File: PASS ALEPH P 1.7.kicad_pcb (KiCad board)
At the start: 2 copper layers, 200 x 100 mm, 79 parts, among them Q1 BCX56-16,115, Q10 BCX56-16,115, Q2 BCX53-16,115, Q3 610, Q4 610, Q5 9610, Q6 9610, Q7 610, Q8 610, Q9 BCX53-16,115

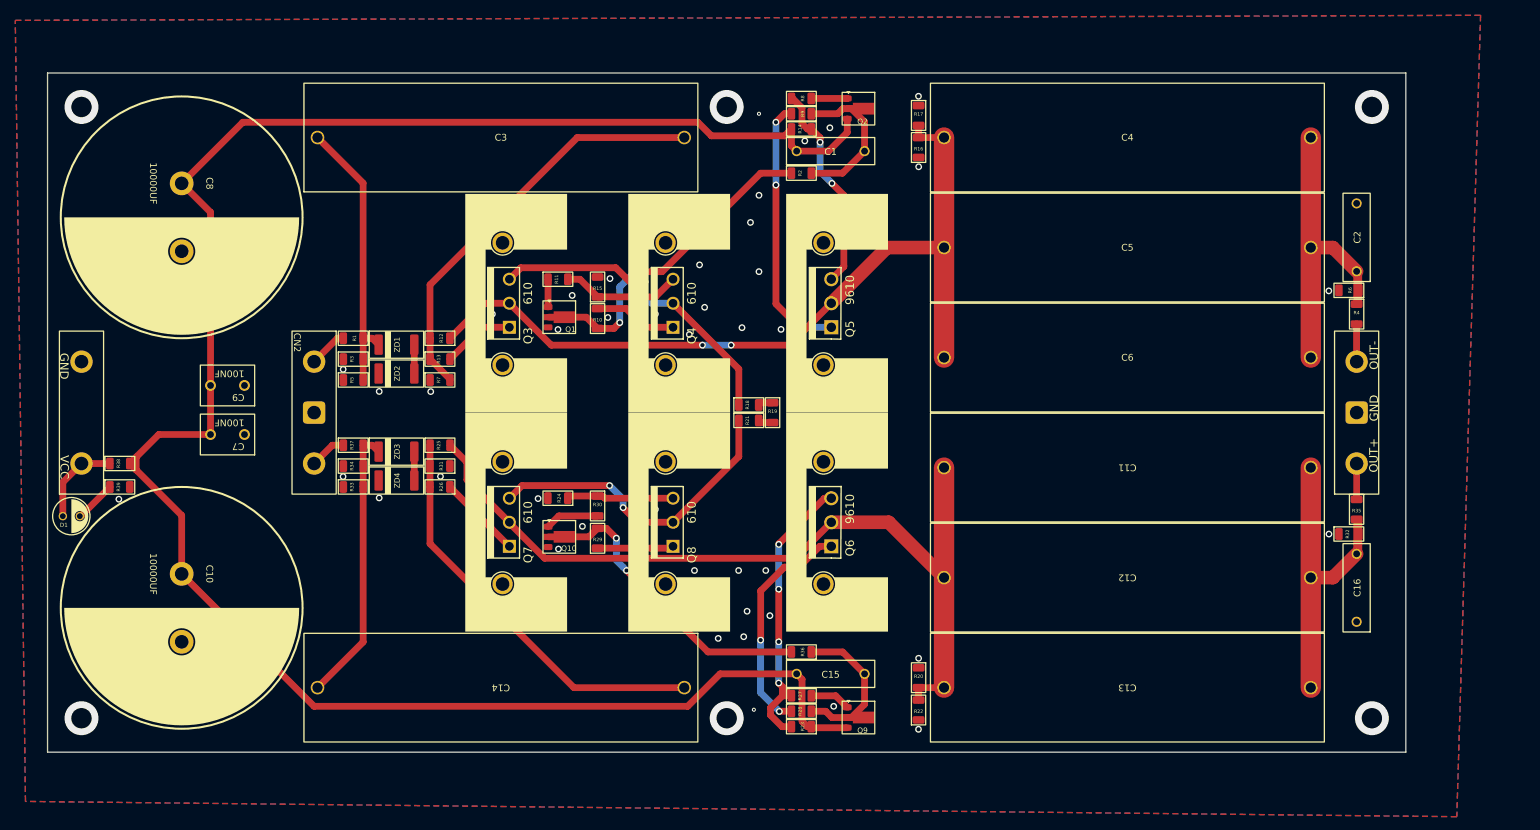
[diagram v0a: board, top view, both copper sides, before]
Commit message: 6 layer-board, layout finished
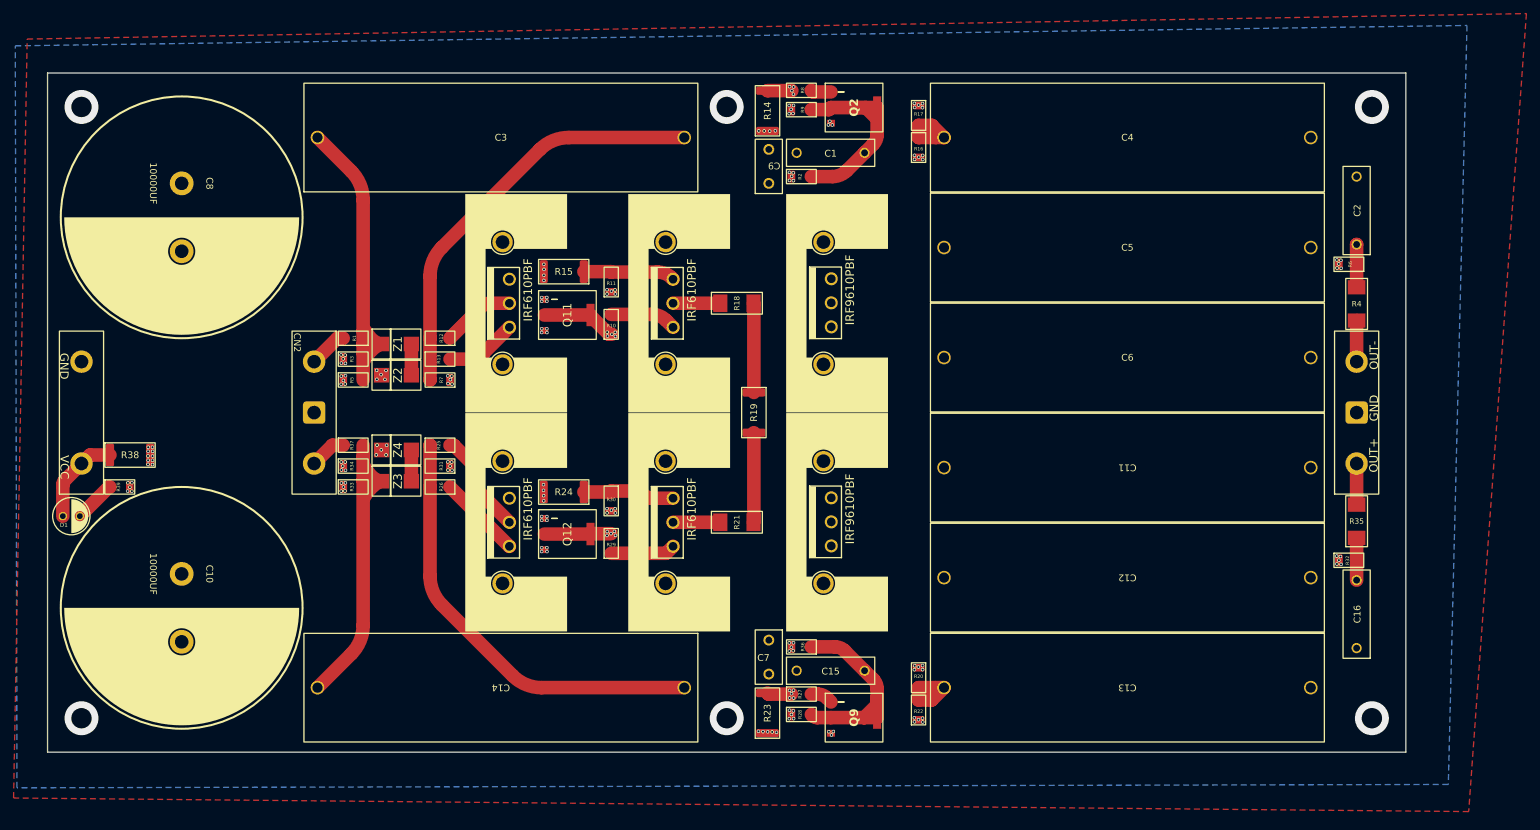
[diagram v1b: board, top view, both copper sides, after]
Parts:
- removed Q1, Q10: BCX56-16,115, 3rd package:BCX56-16,115
- added Q11: BCP56-16,115, cus_transistor:BCP56-16,115, F.Cu at (96.3, 73.4)
- added Q12: BCP56-16,115, cus_transistor:BCP56-16,115, F.Cu at (96.3, 105.6)
- C7, C9: footprint 3rd package:MES104J2A-7-50R0 -> cus_capacitor:MES104J2A-7-50R0
- Q2, Q9: footprint 3rd package:BCX53-16,115 -> cus_transistor:BCP53-16,115
- Q3, Q4, Q7, Q8: value 610 -> IRF610PBF; footprint 3rd package:IRF610PBF -> cus_mosfet:IRF610PBF
- Q5, Q6: value 9610 -> IRF9610PBF; footprint 3rd package:IRF9610PBF -> cus_mosfet:IRF9610PBF
- R1, R37: value 0 -> 10K
- R14, R23, R38: footprint generic package:R_1206 -> generic package:R 2512
- R15, R24: value 33.1 -> 33.2; footprint generic package:R_1206 -> generic package:R 2512
- R18, R21, R35, R4: footprint generic package:R_1206 -> cus_resistor:R_MELF_0207
- R19: footprint generic package:R_1206 -> cus_resistor:R_2512
- Z1: renamed from ZD1; value ZMY9V1-GS08 -> 1SMB5924BT3G; footprint 3rd package:ZMY9V1-GS08 -> cus_zener:1SMB5924BT3G
- Z2: renamed from ZD2; value ZMY9V1-GS08 -> 1SMB5924BT3G; footprint 3rd package:ZMY9V1-GS08 -> cus_zener:1SMB5924BT3G
- Z3: renamed from ZD3; value ZMY9V1-GS08 -> 1SMB5924BT3G; footprint 3rd package:ZMY9V1-GS08 -> cus_zener:1SMB5924BT3G
- Z4: renamed from ZD4; value ZMY9V1-GS08 -> 1SMB5924BT3G; footprint 3rd package:ZMY9V1-GS08 -> cus_zener:1SMB5924BT3G
- moved C7 82.9 mm to (126.0, 121.2), turned to -90 degrees
- moved C9 82.7 mm to (126.0, 54.0), turned to 90 degrees
- moved R21 15.1 mm to (121.2, 103.9)
- moved R18 15.1 mm to (121.2, 71.7)
- moved R11 7.86 mm to (102.8, 68.5), turned to 90 degrees
- moved R23 5.08 mm to (125.8, 135.0), turned to 90 degrees
- moved R14 5.00 mm to (125.8, 46.3), turned to 90 degrees
- moved Z4 4.50 mm to (71.1, 93.2)
- moved Z3 4.35 mm to (71.1, 97.8)
- moved R19 4.05 mm to (123.8, 84.8)
- moved C2 3.95 mm to (212.5, 58.0)
- moved R24 3.93 mm to (98.7, 99.4)
- moved C16 3.88 mm to (212.5, 117.4)
- moved R32 3.87 mm to (211.4, 109.5)
- moved R6 3.84 mm to (211.4, 65.9)
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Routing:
- net Net-(Q2-E): track 297.6 -> 0.00 mm, vias 0 -> 25
- net Net-(Q3-D): track 121.3 -> 20.8 mm, vias 2 -> 0
- net Net-(Q6-D): track 124.8 -> 25.2 mm
- net Net-(C11-Pad1): track 51.0 -> 6.23 mm
- net Net-(C2-Pad1): track 50.5 -> 6.31 mm
- net Net-(Q7-S): track 46.8 -> 35.2 mm, vias 2 -> 0
- net Net-(R19-Pad2): track 2.17 -> 13.2 mm
- net Net-(R18-Pad2): track 2.17 -> 13.2 mm
- net Net-(Q3-S): track 46.0 -> 36.0 mm, vias 1 -> 0
- net Net-(Q9-C): track 22.7 -> 30.3 mm
- net Net-(Q2-C): track 22.5 -> 29.9 mm
- net Net-(Q11-B): track 4.09 -> 10.6 mm, vias 0 -> 9
- net Net-(Q6-S): track 43.6 -> 37.2 mm, vias 4 -> 5
- net Net-(Q5-S): track 31.0 -> 36.8 mm, vias 2 -> 4
- net Net-(Q4-S): track 17.6 -> 13.5 mm
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- added copper zone on In1.Cu, net GND
- added copper zone on In2.Cu, net GND
- added copper zone on In3.Cu, net GND
- added copper zone on In4.Cu, net GND
- added copper zone on In4.Cu, net Net-(C11-Pad1)
- added copper zone on In4.Cu, net Net-(C2-Pad1)
- added copper zone on In4.Cu, net Net-(Q2-E)
- added copper zone on In4.Cu, net Net-(Q3-D)
- added copper zone on In4.Cu, net Net-(Q6-D)
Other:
- copper layers 2 -> 6

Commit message: replace some film resistor, fix some bug
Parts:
- R1, R16, R2, R22, R36, R37: footprint generic package:R_1206 -> cus_resistor:R_MELF_0207
- R14, R23: value 22.1 -> 22; footprint generic package:R 2512 -> cus_resistor:R_MELF_0207
- R15, R24: value 33.2 -> 33; footprint generic package:R 2512 -> cus_resistor:R_MELF_0207
- R38: footprint generic package:R 2512 -> cus_resistor:R_MELF_0207
- moved R17 7.48 mm to (147.5, 51.5), turned to 90 degrees
- moved R37 6.10 mm to (63.2, 98.5)
- moved R16 4.00 mm to (147.5, 44.8), turned to -90 degrees
- moved R33 3.70 mm to (64.8, 95.0)
- moved R34 3.38 mm to (64.8, 92.2)
- moved R14 3.28 mm to (125.8, 43.0)
- moved R23 3.21 mm to (125.8, 131.8)
- moved R38 3.01 mm to (31.9, 94.0)
- moved CN2 3.00 mm to (56.0, 80.2)
- moved R20 2.95 mm to (147.5, 123.9)
- moved R15 2.91 mm to (95.8, 67.0)
- moved R24 2.91 mm to (95.8, 99.4)
- moved R2 1.64 mm to (132.3, 53.5)
- moved R36 1.60 mm to (132.3, 121.9)
- moved R1 1.57 mm to (63.2, 77.0)
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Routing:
- net Net-(Q6-D): track 25.2 -> 15.1 mm
- net Net-(Q3-D): track 20.8 -> 10.8 mm
- net Net-(C14-Pad1): track 64.4 -> 58.5 mm, vias 0 -> 15
- net Net-(C3-Pad2): track 62.1 -> 58.6 mm, vias 0 -> 15
- net Net-(Q9-C): track 30.3 -> 28.0 mm
- net Net-(Q2-C): track 29.9 -> 27.7 mm
- net Net-(Q11-C): track 51.7 -> 52.8 mm, vias 10 -> 13
- net Net-(Q5-S): track 36.8 -> 37.6 mm, vias 4 -> 5
- net Net-(Q6-G): track 29.8 -> 30.5 mm
- net Net-(Q12-C): track 44.2 -> 44.8 mm, vias 10 -> 13
- net Net-(Q5-G): track 35.8 -> 35.2 mm
- net /IN-: track 5.41 -> 6.00 mm, vias 0 -> 8
- net Net-(Z1-K): track 40.9 -> 41.5 mm, vias 0 -> 26
- net Net-(Q4-S): track 13.5 -> 14.0 mm
- net /IN+: track 5.72 -> 6.25 mm, vias 0 -> 8
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- added copper zone on F.Cu, net Net-(Q3-D)
- added copper zone on F.Cu, net Net-(Q6-D)

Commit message: fix some bug
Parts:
- added JJC***: LOGO, generic package:LOGO, F.Cu at (33.8, 80.2)

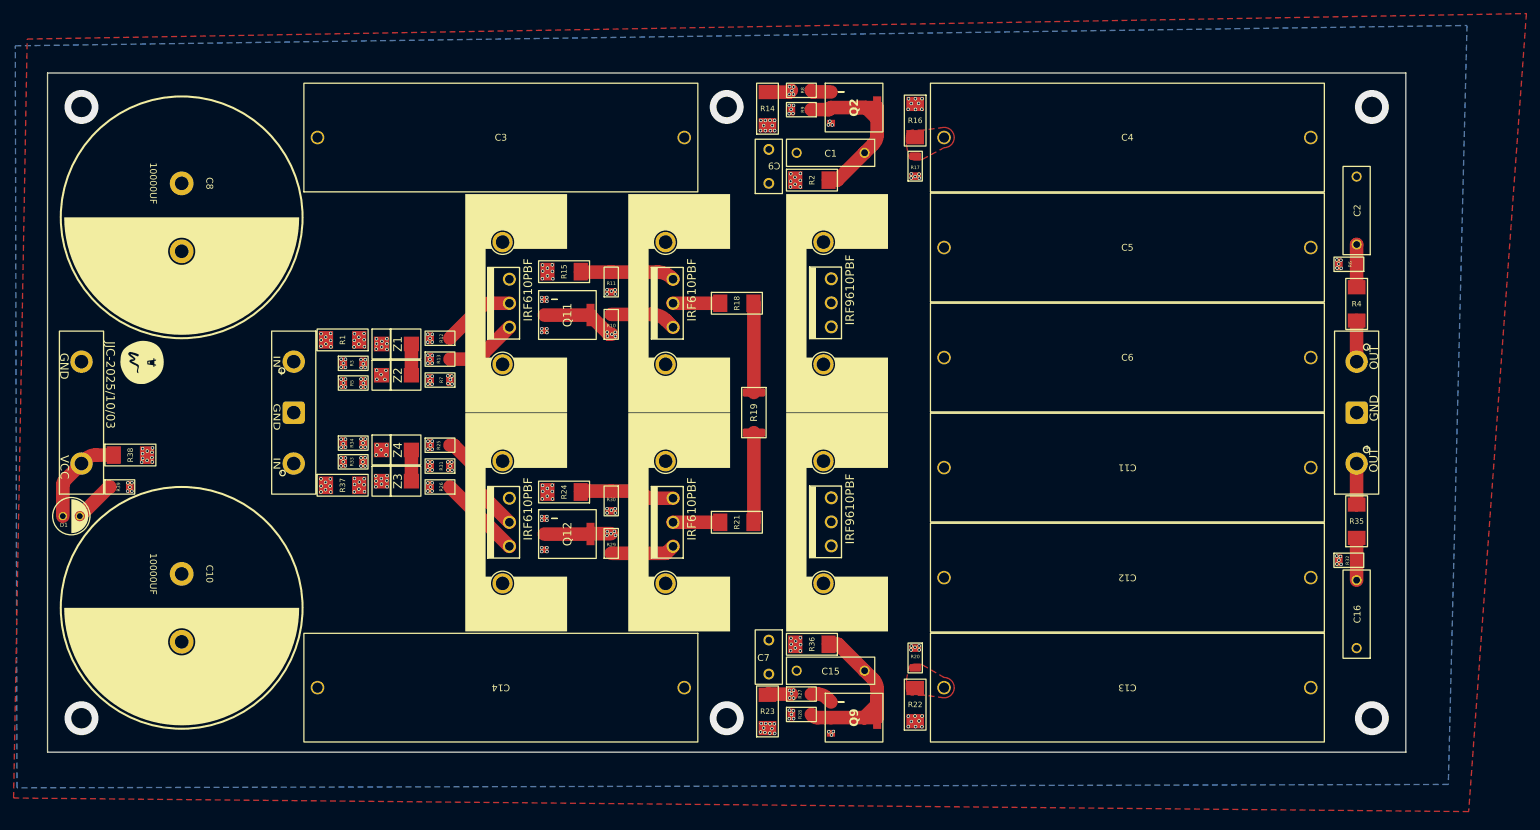
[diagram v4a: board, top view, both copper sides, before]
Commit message: split some gnd pin, fix some bug
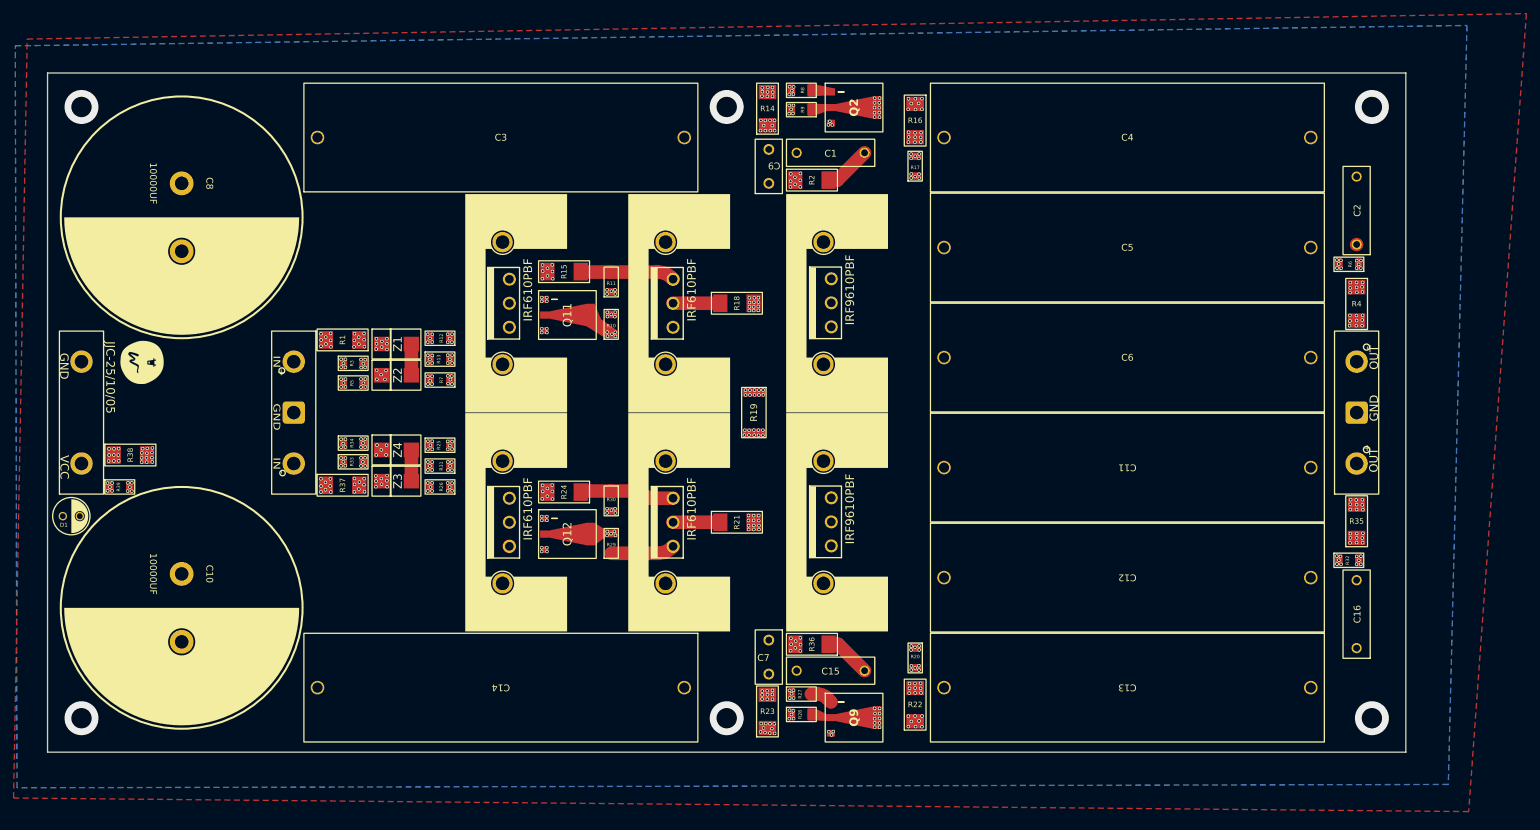
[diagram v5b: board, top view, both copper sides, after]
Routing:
- net Net-(Q2-C): track 27.7 -> 15.5 mm, vias 0 -> 10
- net Net-(Q11-C): track 52.8 -> 41.9 mm
- net Net-(Q12-C): track 44.8 -> 34.7 mm
- net Net-(Q9-C): track 28.0 -> 18.6 mm, vias 0 -> 10
- net Net-(C2-Pad1): track 6.31 -> 0.01 mm, vias 0 -> 14
- net Net-(C11-Pad1): track 6.23 -> 0.00 mm, vias 0 -> 14
- net Net-(Q2-B): track 3.00 -> 0.00 mm
- net /VCC: track 14.0 -> 16.6 mm, vias 0 -> 9
- net Net-(Q6-S): track 37.2 -> 39.2 mm, vias 5 -> 14
- net Net-(Q5-S): track 37.6 -> 39.3 mm, vias 5 -> 14
- net Net-(Q7-G): track 12.4 -> 13.6 mm, vias 0 -> 5
- net Net-(R18-Pad2): track 13.2 -> 14.0 mm, vias 0 -> 22
- net Net-(R19-Pad2): track 13.2 -> 13.7 mm, vias 0 -> 22
- net Net-(Q6-D): track 15.1 -> 14.7 mm, vias 0 -> 19
- net Net-(Q3-D): track 10.8 -> 10.6 mm, vias 0 -> 19
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- added copper zone on In2.Cu, net Net-(Q3-D)
- added copper zone on In2.Cu, net Net-(Q6-D)
- removed copper zone on F.Cu, net Net-(Q3-D)
- removed copper zone on F.Cu, net Net-(Q6-D)
